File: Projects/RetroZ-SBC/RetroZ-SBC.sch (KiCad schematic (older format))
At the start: 60 parts, among them IC1 PO_RESET, IC2 AT28C256B-15PU, IC3 AS6C62256-55PCN, J1 02x20, J2 User Port A, J3 User Port B, J4 IEI SELECT, J5 USB_OTG, J6 CLOCK DIV., SW1 RESET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

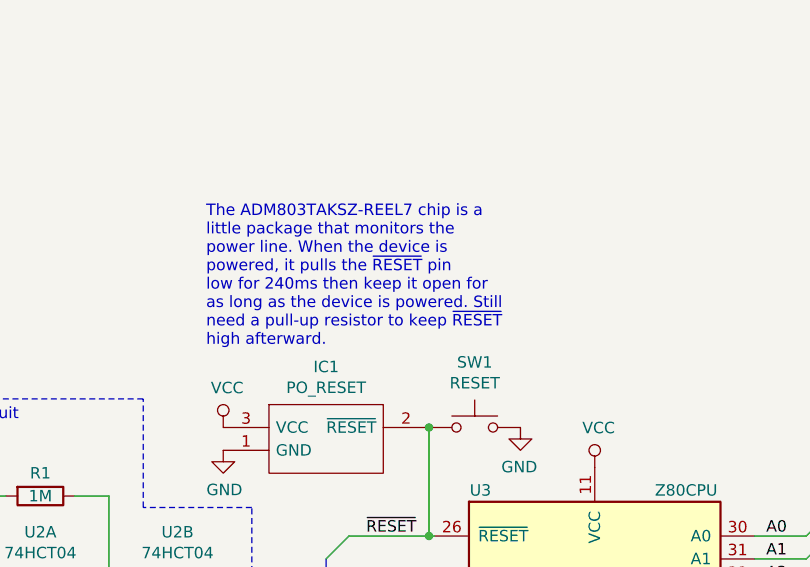
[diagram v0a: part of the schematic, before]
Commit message: added the template
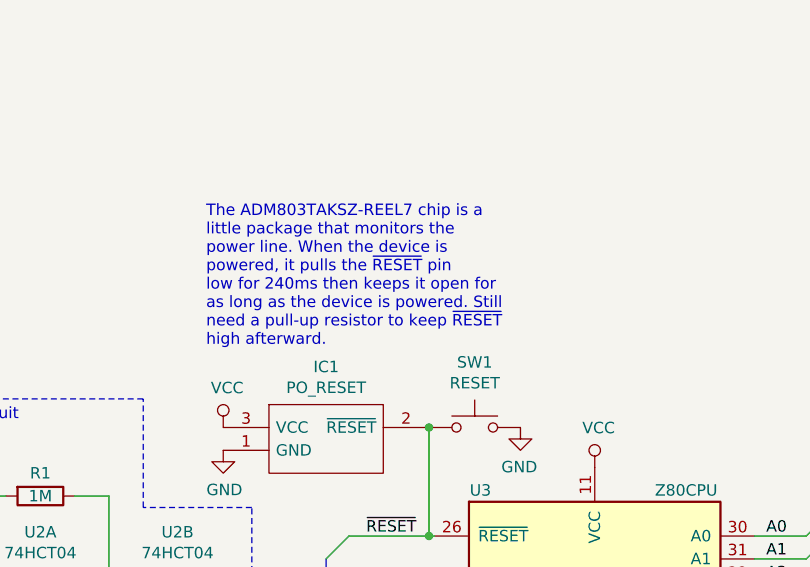
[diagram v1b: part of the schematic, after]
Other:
- note added: "The ADM803TAKSZ-REEL7 chip is a \nlittle package that monitors the \npower line. When the device is \npowered, it pulls the ~RESET~ pin \nlow for 240ms then keeps it open for\nas long as the device is powered. Still\nneed a pull-up resistor to keep ~RESET~\nhigh afterward."
- note removed: "The ADM803TAKSZ-REEL7 chip is a \nlittle package that monitors the \npower line. When the device is \npowered, it pulls the ~RESET~ pin \nlow for 240ms then keep it open for\nas long as the device is powered. Still\nneed a pull-up resistor to keep ~RESET~\nhigh afterward."
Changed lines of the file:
@@
 	10325 1575 10325 1650
 Text Notes 2975 2500 0    50   ~ 0
-The ADM803TAKSZ-REEL7 chip is a \nlittle package that monitors the \npower line. When the device is \npowered, it pulls the ~RESET~ pin \nlow for 240ms then keep it open for\nas long as the device is powered. Still\nneed a pull-up resistor to keep ~RESET~\nhigh afterward.
+The ADM803TAKSZ-REEL7 chip is a \nlittle package that monitors the \npower line. When the device is \npowered, it pulls the ~RESET~ pin \nlow for 240ms then keeps it open for\nas long as the device is powered. Still\nneed a pull-up resistor to keep ~RESET~\nhigh afterward.
 Wire Wire Line
 	3600 3325 3950 3325
@@
 Wire Notes Line
 	2700 2725 1675 2725
+Wire Notes Line
+	1675 2725 1675 4950
+Text Notes 1725 2825 0    50   ~ 0
+Clock Circuit
 Wire Wire Line
 	7325 8575 7825 8575
 Wire Wire Line
 	7325 8175 7975 8175
-Wire Notes Line
-	1675 2725 1675 4950
 Wire Bus Line
 	7925 5925 7925 9550
@@
 Wire Bus Line
 	8475 2900 8475 6650
-Text Notes 1725 2825 0    50   ~ 0
-Clock Circuit
 $EndSCHEMATC

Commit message: Created the schematic
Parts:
- R12: value 10K -> 2K
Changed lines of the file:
@@
 P 6475 5625
 F 0 "R12" H 6325 5775 50  0000 L CNN
-F 1 "10K" V 6475 5550 50  0000 L CNN
+F 1 "2K" V 6475 5575 50  0000 L CNN
 F 2 "Resistors_THT:R_Axial_DIN0207_L6.3mm_D2.5mm_P10.16mm_Horizontal" V 6405 5625 50  0001 C CNN
 F 3 "~" H 6475 5625 50  0001 C CNN
